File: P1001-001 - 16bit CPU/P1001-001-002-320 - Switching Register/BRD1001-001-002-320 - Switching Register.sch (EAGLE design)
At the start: 28 parts, among them IC1 74HC173D, IC12 74AC245DW, IC13 74ALS02D, IC14 74ALS00D, IC15 74ALS04D, IC17 74ALS02D, IC18 74ALS04D, IC19 74ALS02D, IC2 74HC173D, IC27 MEGA8535-A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

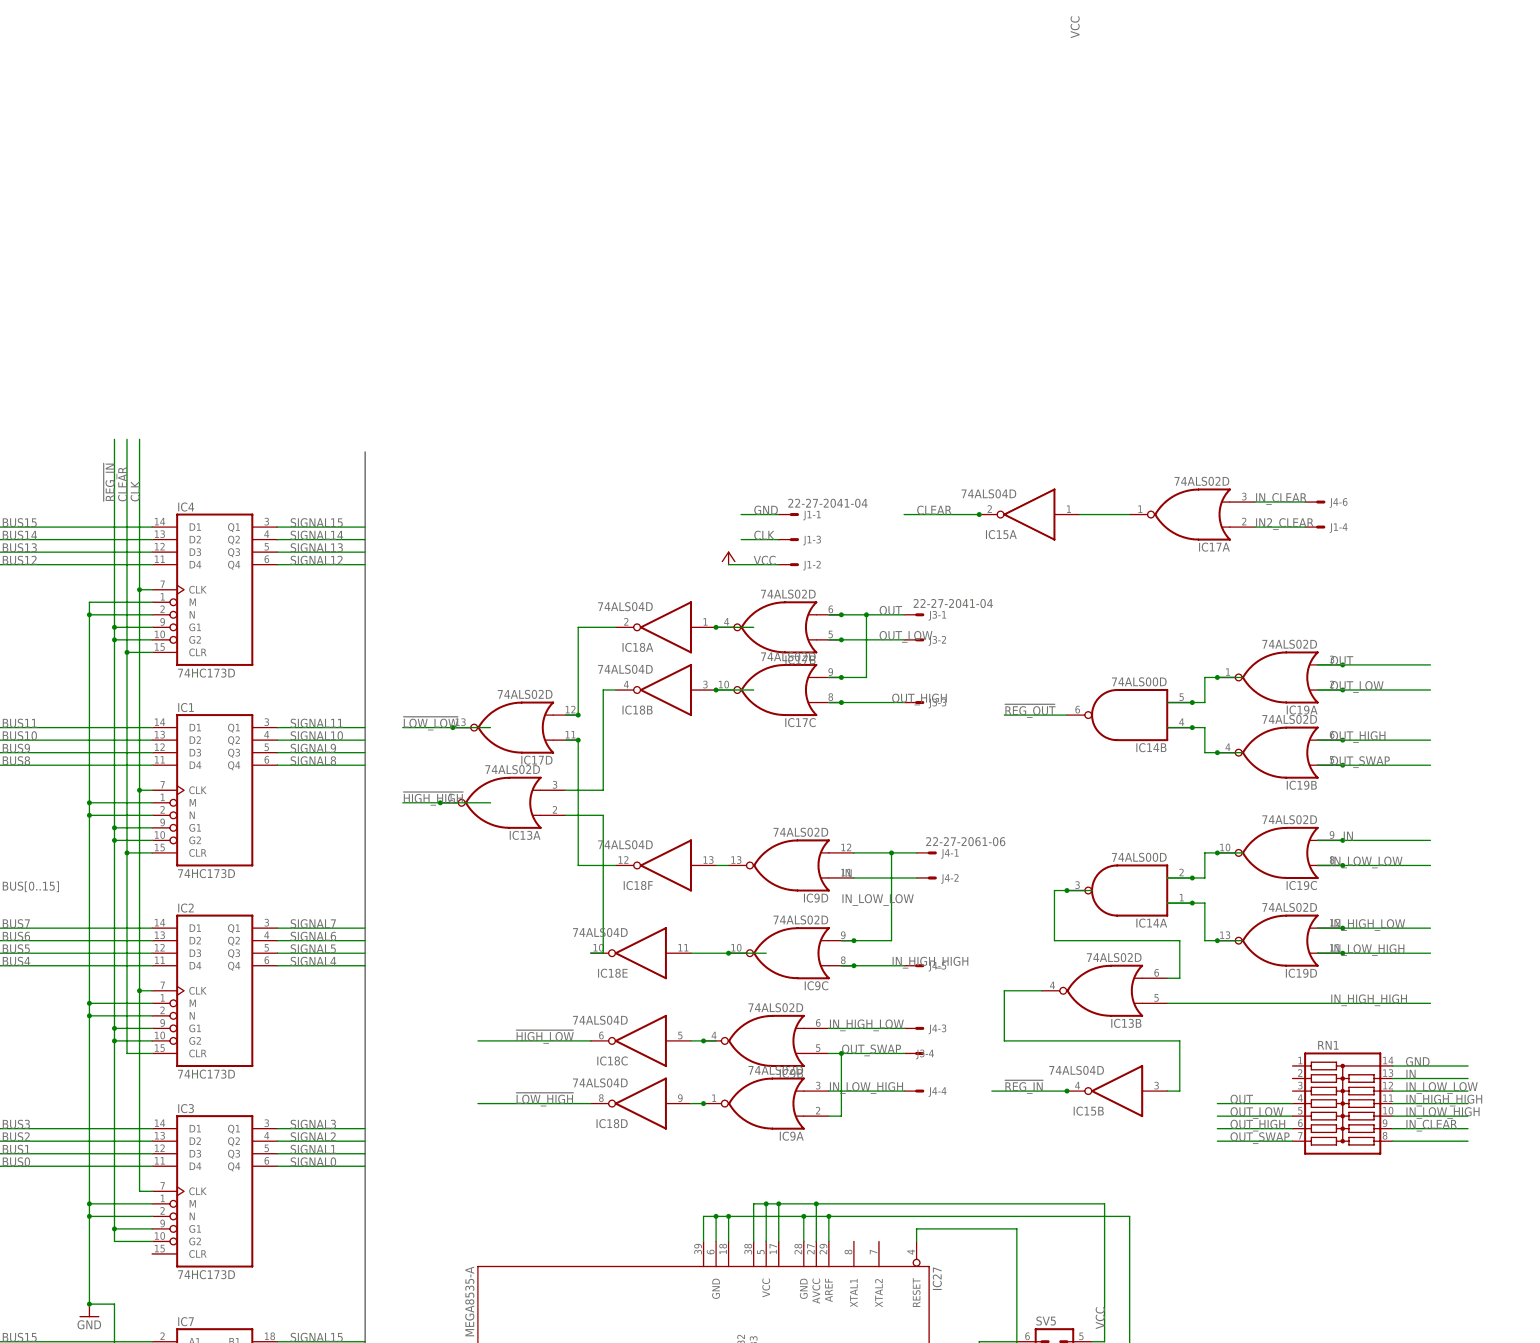
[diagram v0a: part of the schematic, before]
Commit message: Added the simple reg, cleaned things up
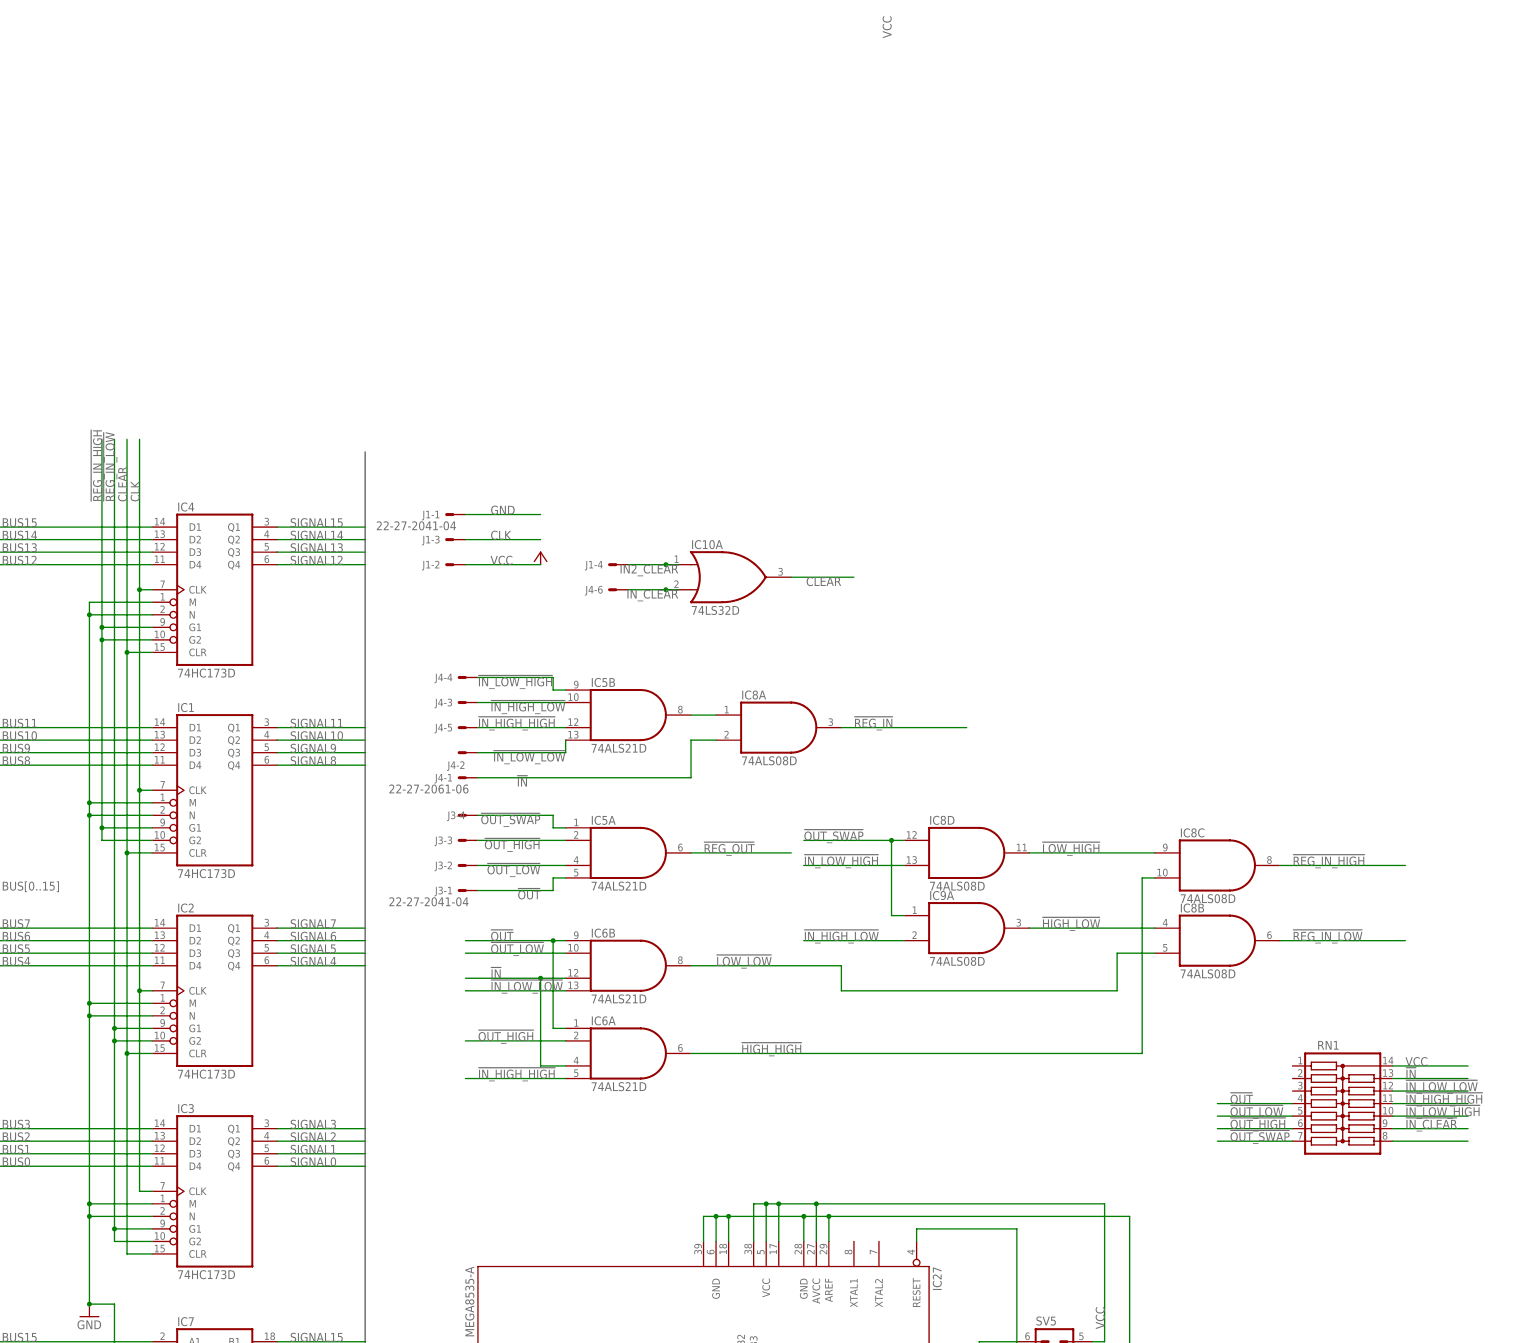
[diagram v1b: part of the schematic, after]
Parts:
- removed IC13, IC17, IC19: 74ALS02D, 74xx-us:74ALS02D
- removed IC14: 74ALS00D, 74xx-us:74ALS00D
- removed IC15, IC18: 74ALS04D, 74xx-us:74ALS04D
- added IC10: 74LS32D, 74xx-us:74LS32D
- added IC5, IC6: 74ALS21D, 74xx-us:74ALS21D
- added IC8: 74ALS08D, 74xx-us:74ALS08D
- IC9: value 74ALS02D -> 74ALS08D; device 74xx-us:74ALS02D -> 74xx-us:74ALS08D
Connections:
- removed net IN: IC19C.I1, IC9C.I1, IC9D.I1, J4-1.S, RN1.13
- removed net IN_HIGH_HIGH: IC13B.I0, IC9C.I0, J4-5.S, RN1.11
- removed net IN_HIGH_LOW: IC19D.I1, IC9B.I1, J4-3.S
- removed net IN_LOW_HIGH: IC19D.I0, IC9A.I1, J4-4.S, RN1.10
- removed net IN_LOW_LOW: IC19C.I0, IC9D.I0, J4-2.S, RN1.12
- removed net N$10: IC17D.I1, IC18A.O
- removed net N$11: IC17D.I0, IC18F.O
- removed net N$12: IC13A.I1, IC18B.O
- removed net N$13: IC13A.I0, IC18E.O
- removed net N$14: IC18C.I, IC9B.O
- removed net N$15: IC18D.I, IC9A.O
- removed net N$16: IC13B.I1, IC14A.O
- removed net N$17: IC13B.O, IC15B.I
- removed net N$2: IC17C.O, IC18B.I
- removed net N$3: IC14A.I1, IC19C.O
- removed net N$4: IC14A.I0, IC19D.O
- removed net N$5: IC15A.I, IC17A.O
- removed net N$6: IC18F.I, IC9D.O
- removed net N$7: IC14B.I1, IC19A.O
- removed net N$8: IC14B.I0, IC19B.O
- removed net N$9: IC18E.I, IC9C.O
- removed net OUT: IC17B.I1, IC17C.I1, IC19A.I1, J3-1.S, RN1.4
- removed net OUT_HIGH: IC17C.I0, IC19B.I1, J3-3.S, RN1.6
- removed net OUT_LOW: IC17B.I0, IC19A.I0, J3-2.S, RN1.5
- removed net OUT_SWAP: IC19B.I0, IC9A.I0, IC9B.I0, J3-4.S, RN1.7
- new net !IN: IC6A.I2, IC6B.I2, IC8A.I1, J4-1.S, RN1.13
- new net !IN_CLEAR: RN1.9
- new net !IN_HIGH_HIGH: IC5B.I2, IC6A.I3, J4-5.S, RN1.11
- new net !IN_HIGH_LOW: IC5B.I1, IC9A.I1, J4-3.S
- new net !IN_LOW_HIGH: IC5B.I0, IC8D.I1, J4-4.S, RN1.10
- new net !IN_LOW_LOW: IC5B.I3, IC6B.I3, J4-2.S, RN1.12
- new net !OUT: IC5A.I3, IC6A.I0, IC6B.I0, J3-1.S, RN1.4
- new net !OUT_HIGH: IC5A.I1, IC6A.I1, J3-3.S, RN1.6
- new net !OUT_LOW: IC5A.I2, IC6B.I1, J3-2.S, RN1.5
- new net !OUT_SWAP: IC5A.I0, IC8D.I0, IC9A.I0, J3-4.S, RN1.7
- new net !REG_IN_HIGH: IC1A.G1, IC1A.G2, IC4A.G1, IC4A.G2, IC8C.O
- new net !REG_IN_LOW: IC2A.G1, IC2A.G2, IC3A.G1, IC3A.G2, IC8B.O
- net !HIGH_HIGH: now also IC6A.O, IC8C.I1; no longer IC13A.O
- net !HIGH_LOW: now also IC8B.I0, IC9A.O; no longer IC18C.O
- net !LOW_HIGH: now also IC8C.I0, IC8D.O; no longer IC18D.O
- net !LOW_LOW: now also IC6B.O, IC8B.I1; no longer IC17D.O
- net !REG_IN: now also IC8A.O; no longer IC15B.O, IC1A.G1, IC1A.G2, IC2A.G1, IC2A.G2, IC3A.G1, IC3A.G2, IC4A.G1, IC4A.G2
- net !REG_OUT: now also IC5A.O; no longer IC14B.O
- net CLEAR: now also IC10A.O, IC3A.CLR; no longer IC15A.O
- net GND: no longer RN1.14
- net IN2_CLEAR: now also IC10A.I0; no longer IC17A.I0
- net IN_CLEAR: now also IC10A.I1; no longer IC17A.I1, RN1.9
- net N$1: now also IC5B.O, IC8A.I0; no longer IC17B.O, IC18A.I
- net VCC: now also RN1.14
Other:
- moved on the sheet: J1-1, J1-2, J1-3, J1-4, J3-1, J3-2, J3-3, J3-4, J4-1, J4-2, J4-3, J4-4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

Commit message: Finished All Boards
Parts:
- added C1, C2, C3, C4: 1uF, rcl:C-USC1206
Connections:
- net GND: now also C1.2, C2.2, C3.2, C4.2
- net VCC: now also C1.1, C2.1, C3.1, C4.1

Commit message: Fix problems with registers
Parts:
- removed C1, C2: 1uF, rcl:C-USC1206
- removed IC9: 74ALS08D, 74xx-us:74ALS08D
- removed RN1: (no value), resistor-dil:13RSOMC
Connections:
- removed net !IN_CLEAR: RN1.9
- removed net !REG_IN: IC8A.O
- removed net N$1: IC5B.O, IC8A.I0
- removed net N$23: RN1.8
- net !HIGH_HIGH: now also IC8D.I1; no longer IC8C.I1
- net !HIGH_LOW: now also IC8B.O, IC8C.I0; no longer IC8B.I0, IC9A.O
- net !IN: no longer IC8A.I1, RN1.13
- net !IN_HIGH_HIGH: no longer IC5B.I2, RN1.11
- net !IN_HIGH_LOW: now also IC8B.I1; no longer IC5B.I1, IC9A.I1
- net !IN_LOW_HIGH: now also IC8A.I1; no longer IC5B.I0, IC8D.I1, RN1.10
- net !IN_LOW_LOW: no longer IC5B.I3, RN1.12
- net !LOW_HIGH: now also IC8A.O, IC8D.I0; no longer IC8C.I0, IC8D.O
- net !LOW_LOW: now also IC8C.I1; no longer IC8B.I1
- net !OUT: no longer RN1.4
- net !OUT_HIGH: no longer RN1.6
- net !OUT_LOW: no longer RN1.5
- net !OUT_SWAP: now also IC8A.I0, IC8B.I0; no longer IC8D.I0, IC9A.I0, RN1.7
- net !REG_IN_LOW: now also IC8D.O; no longer IC8B.O
- net GND: no longer C1.2, C2.2
- net VCC: no longer C1.1, C2.1, RN1.14
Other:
- moved on the sheet: IC8A, IC8B, IC8C, IC8D
